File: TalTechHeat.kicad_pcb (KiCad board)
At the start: 4 copper layers, 100 x 30 mm, 74 parts, among them J1 02x03, J2 OLED_SSD1306, J3 XT-30, Q1 DMP4015SPSQ-13, Q2 PJQ4439EP-AU_R2_002A1, Q3 PJQ4439EP-AU_R2_002A1, Q4 IRLR8726TRPBF, Q5 SS8050-G, SW1 Reset_Switch, SW2 BUT1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

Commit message: Updated changes Rev 1.1
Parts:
- moved C1 6.56 mm to (179.9, 92.6), turned to 90 degrees
- moved C2 1.43 mm to (182.4, 92.6)
- moved Q5 1.11 mm to (203.6, 91.6), turned to 0 degrees
- moved C3 0.35 mm to (163.1, 94.5)
- moved C4 0.35 mm to (168.7, 94.5)
- moved L1 0.35 mm to (174.1, 94.5)
- moved R2 0.35 mm to (167.7, 89.0)
- moved R1 0.35 mm to (164.0, 89.0)
- moved U2 0.35 mm to (166.1, 94.5)
- moved R4 0.22 mm to (189.1, 105.1)
- moved R3 0.20 mm to (189.1, 106.6)
- moved C18 0.10 mm to (198.7, 98.9)
- moved D4 0.08 mm to (187.8, 95.1)
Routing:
- net +3.3V: track 212.2 -> 35.7 mm, vias 2 -> 19
- net GND: track 0.00 -> 18.6 mm, vias 133 -> 156
- net /U_P: track 31.2 -> 26.1 mm, vias 1 -> 0
- net /U_N: track 32.4 -> 29.8 mm, vias 1 -> 0
- net /CC2: track 50.1 -> 48.7 mm, vias 2 -> 3
- added copper zone on F.Cu, net +3.3V
- added copper zone on In2.Cu, net +3.3V
- removed copper zone on In2.Cu, net GND

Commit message: Rev 1.2
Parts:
- moved R7 17.6 mm to (237.2, 112.5), turned to 180 degrees
- moved R6 6.72 mm to (232.8, 112.5), turned to 180 degrees
- moved D1 1.49 mm to (228.7, 110.8), turned to 90 degrees
- moved C10 0.93 mm to (175.0, 111.2), turned to 180 degrees
- moved C9 0.80 mm to (174.8, 109.0), turned to 180 degrees
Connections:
- C3 pad 1: +24V_D -> +20V_D
- U2 pad 4: +24V_D -> +20V_D
- U2 pad 5: +24V_D -> +20V_D
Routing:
- net +3.3V: track 35.7 -> 52.6 mm, vias 19 -> 17
- net /VCC-DIV: track 45.9 -> 56.0 mm
- net +24V_D: track 3.09 -> 0.00 mm
- net +20V_D: track 3.41 -> 6.32 mm, vias 0 -> 10
- net +20V: track 39.0 -> 37.1 mm
- net /SDA: track 73.0 -> 73.9 mm
- net /PD_RST: track 39.2 -> 38.5 mm
- net Net-(Q2-G): track 33.0 -> 32.3 mm
- net /CC2: track 48.7 -> 48.2 mm
- net GND: track 18.6 -> 18.7 mm, vias 156 -> 60
- added copper zone on F.Cu, net +20V_D
- added copper zone on In2.Cu, net +20V_D

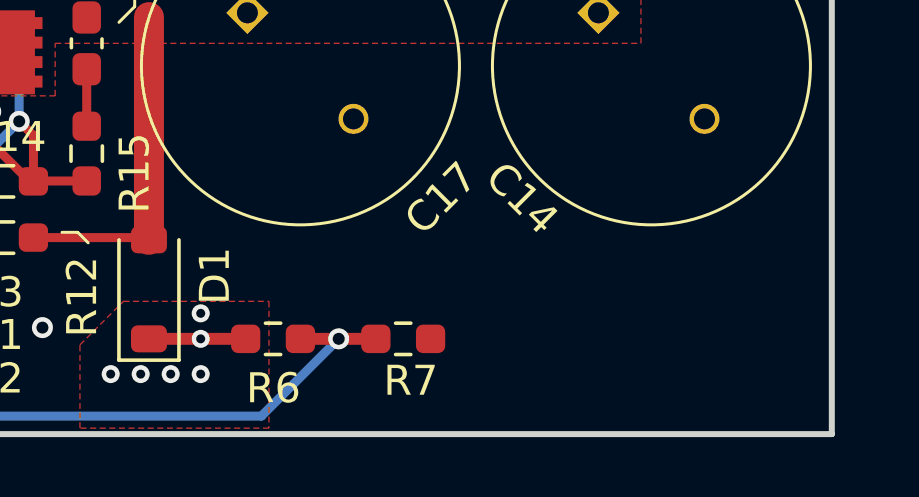
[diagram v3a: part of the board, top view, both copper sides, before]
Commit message: Added the silkscreen as well
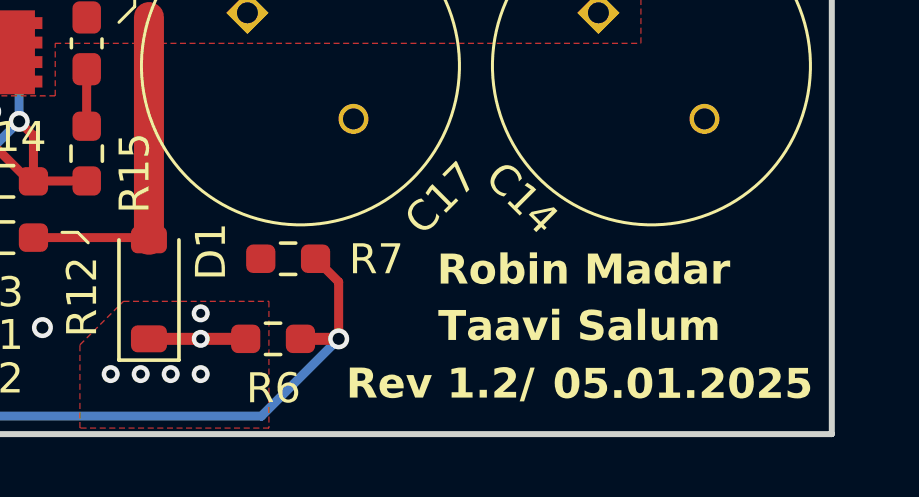
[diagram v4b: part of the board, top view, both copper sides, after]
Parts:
- added G***: LOGO, AA:Taltech, B.Cu at (170.7, 93.4)
- moved R7 4.67 mm to (233.3, 109.8), turned to 0 degrees
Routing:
- net /VCC-DIV: track 56.0 -> 57.8 mm
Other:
- board text added: "05.01.2025"
- board text added: "Rev 1.2/"
- board text added: "Robin Madar"
- board text added: "Taavi Salum"

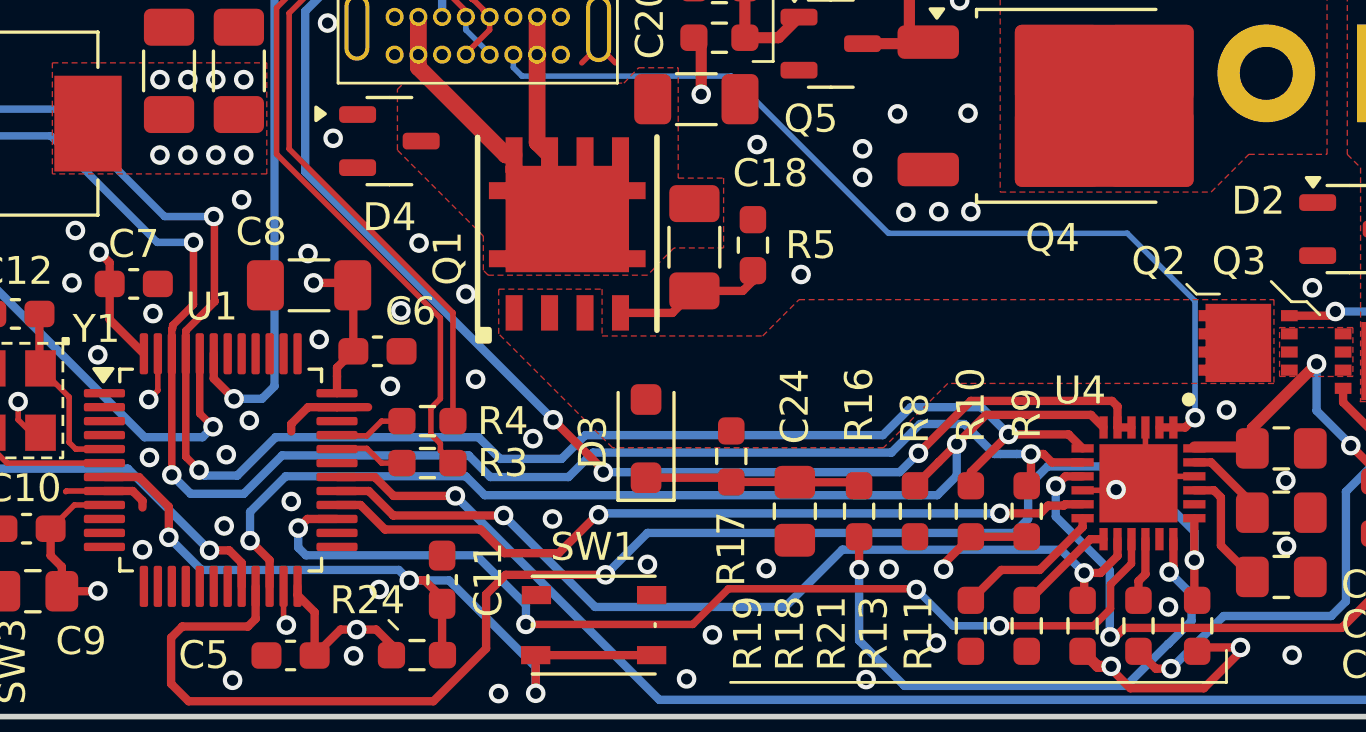
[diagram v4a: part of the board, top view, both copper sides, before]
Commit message: Silckscreen changes and BOM changes
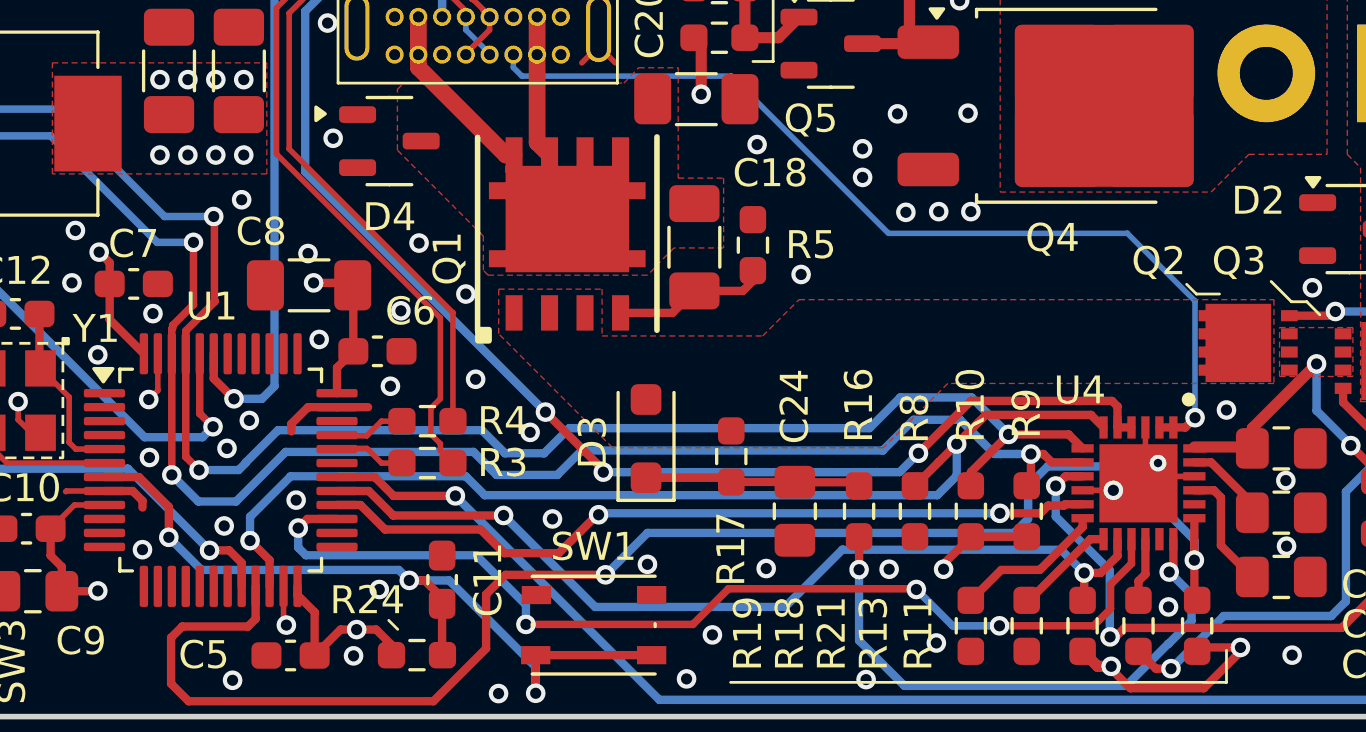
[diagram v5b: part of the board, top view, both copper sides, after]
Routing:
- net GND: track 18.7 -> 18.6 mm, vias 60 -> 61
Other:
- board text added: "Reflow Solder Plate"

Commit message: Rev 1.3, one resistor and exports update
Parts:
- added R27: 1k, Resistor_SMD:R_0603_1608Metric_Pad0.98x0.95mm_HandSolder, F.Cu at (191.7, 104.2)
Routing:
- net /U_P: track 26.1 -> 27.8 mm
- net +3.3V: track 52.6 -> 53.6 mm, vias 17 -> 18
- net GND: vias 61 -> 60
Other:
- board text added: "Rev 1.3/"
- board text removed: "Rev 1.2/"

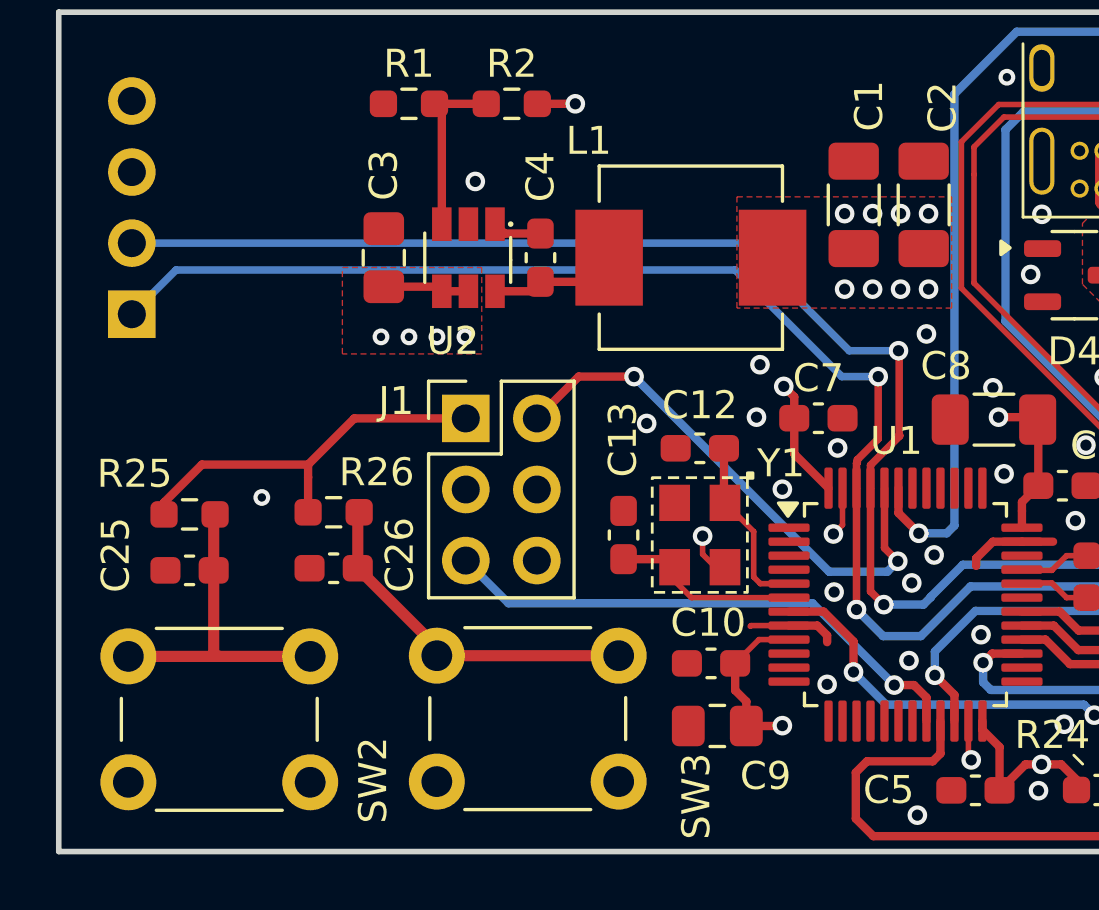
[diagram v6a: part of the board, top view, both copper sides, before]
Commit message: Removed boot1, added UART
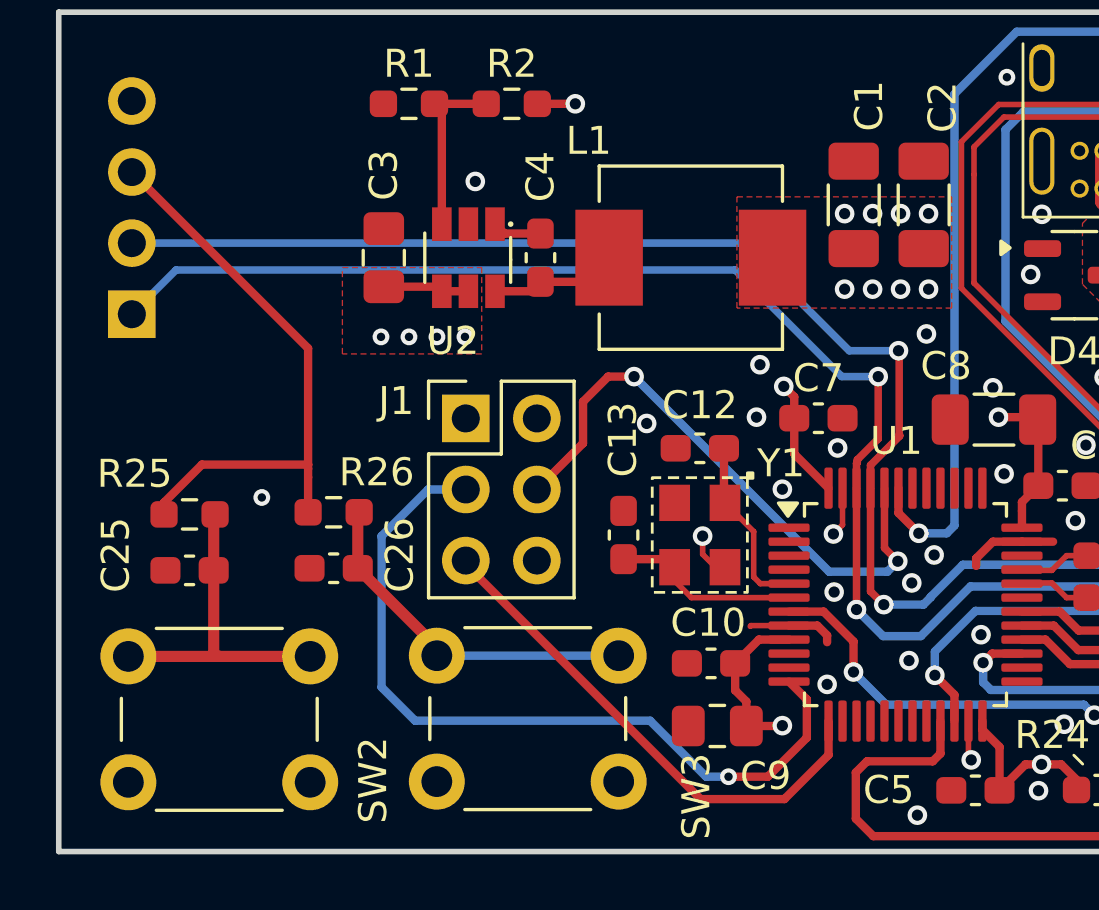
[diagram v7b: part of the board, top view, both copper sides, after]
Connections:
- J1 pad 1: +3.3V -> unconnected-(J1-Pin_1-Pad1)
- J1 pad 2: /BOOT0 -> GND
- J1 pad 3: GND -> /UART2_TX
- J1 pad 4: GND -> /BOOT0
- J1 pad 5: /BOOT1 -> /UART2_RX
- U1 pad 12: unconnected-(U1-PA2-Pad12) -> /UART2_TX
- U1 pad 13: unconnected-(U1-PA3-Pad13) -> /UART2_RX
- U1 pad 20: /BOOT1 -> unconnected-(U1-PB2-Pad20)
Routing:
- net /UART2_TX: track 0.00 -> 28.5 mm, vias 0 -> 1
- net /BOOT1: track 19.3 -> 0.00 mm, vias 1 -> 0
- net /UART2_RX: track 0.00 -> 18.4 mm
- net +3.3V: track 53.6 -> 60.4 mm
- net /BOOT0: track 19.4 -> 21.3 mm

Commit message: TaltechPlate folder Rev1, no Titleblock yet
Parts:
- added J4: Conn_01x04, Connector_JST:JST_PH_B4B-PH-K_1x04_P2.00mm_Vertical, B.Cu at (172.1, 89.2)
- moved G*** 8.16 mm to (162.7, 91.6)
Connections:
- U1 pad 14: unconnected-(U1-PA4-Pad14) -> /TEMP_1
- U1 pad 15: unconnected-(U1-PA5-Pad15) -> /TEMP_2
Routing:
- net /TEMP_1: track 0.00 -> 35.2 mm, vias 0 -> 2
- net /TEMP_2: track 0.00 -> 34.6 mm, vias 0 -> 2
- net /PD_ALERT: track 53.1 -> 50.2 mm
- net GND: vias 60 -> 63
